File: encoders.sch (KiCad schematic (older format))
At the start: 40 parts

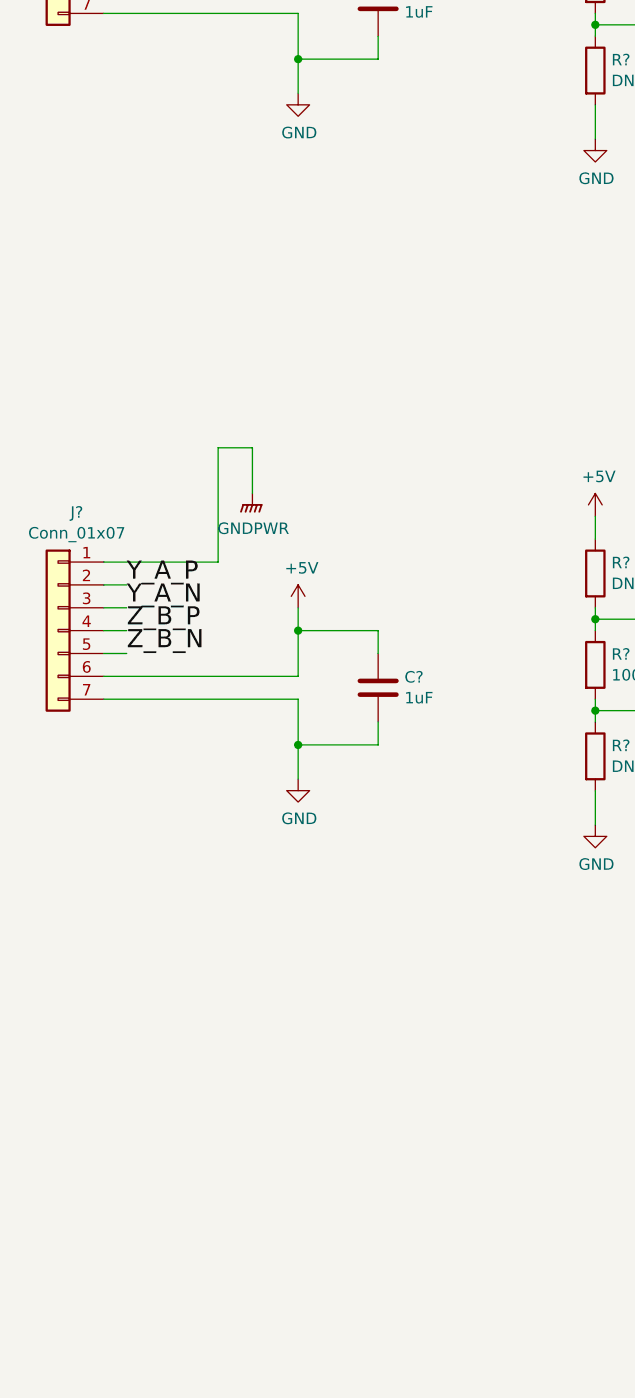
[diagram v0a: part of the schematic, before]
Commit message: Added motor feedback to stm32. added comms/boot to stm32
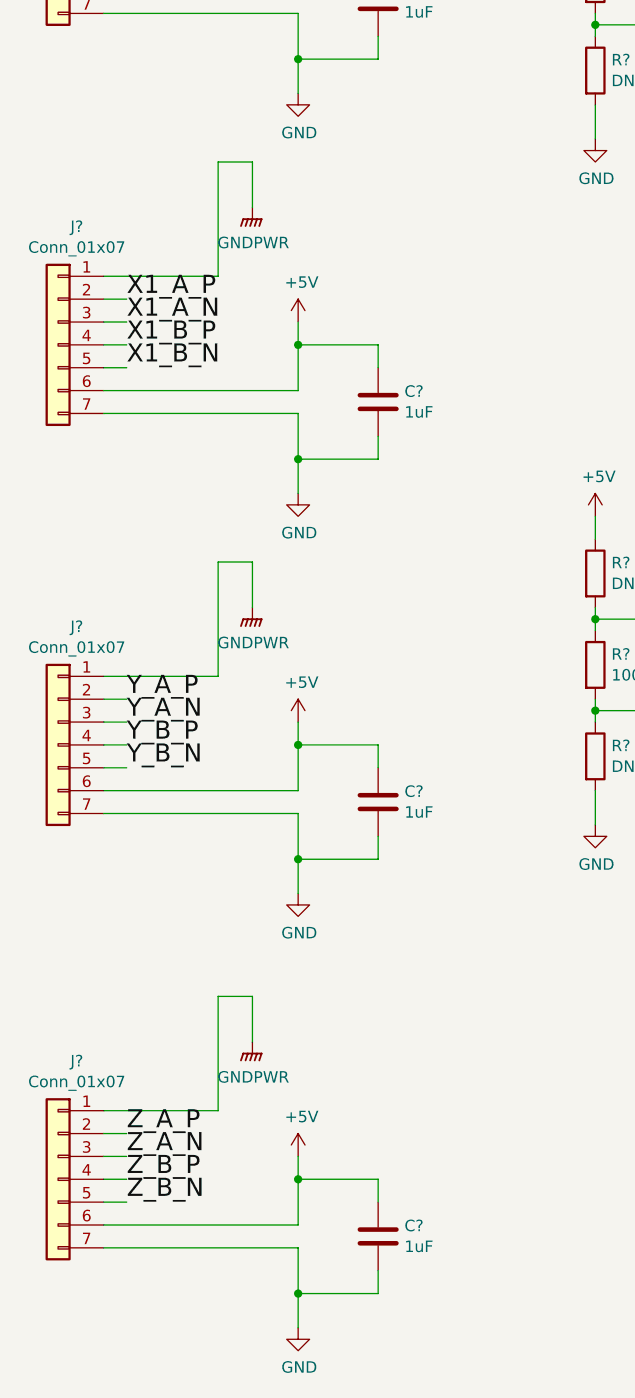
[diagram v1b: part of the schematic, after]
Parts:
- added C? (x2): 1uF, symbol Device:C
- added J? (x2): Conn_01x07, symbol Connector_Generic:Conn_01x07
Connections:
- net +5V: now also C?.1, C?.1, J?.6 (Pin_6), J?.6 (Pin_6)
- net GND: now also C?.2, C?.2, J?.7 (Pin_7), J?.7 (Pin_7)
- net GNDPWR: now also J?.1 (Pin_1), J?.1 (Pin_1)
- net X1_A_N: now also J?.3 (Pin_3)
- net X1_A_P: now also J?.2 (Pin_2)
- net X1_B_N: now also J?.5 (Pin_5)
- net X1_B_P: now also J?.4 (Pin_4)
- net Y_B_N: now also J?.5 (Pin_5)
- net Y_B_P: now also J?.4 (Pin_4)
- net Z_A_N: now also J?.3 (Pin_3)
- net Z_A_P: now also J?.2 (Pin_2)
- net Z_B_N: now also J?.5 (Pin_5); no longer J?.5 (Pin_5)
- net Z_B_P: now also J?.4 (Pin_4); no longer J?.4 (Pin_4)
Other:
- moved on the sheet: C?, J?

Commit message: cleaned encoder rx. removed PU from CoP rst. misc other CoP updates
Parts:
- C?: value C -> 0.1uF; footprint (none) -> Capacitor_SMD:C_0603_1608Metric_Pad1.05x0.95mm_HandSolder
- C?: value C -> 0.1uF
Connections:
- net GND: now also U?.8 (GND), U?.8 (GND)
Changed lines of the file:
@@
 P 10650 700
 F 0 "C?" H 10765 746 50  0000 L CNN
-F 1 "C" H 10765 655 50  0000 L CNN
-F 2 "" H 10688 550 50  0001 C CNN
+F 1 "0.1uF" H 10765 655 50  0000 L CNN
+F 2 "Capacitor_SMD:C_0603_1608Metric_Pad1.05x0.95mm_HandSolder" H 10688 550 50  0001 C CNN
 F 3 "~" H 10650 700 50  0001 C CNN
 	1    10650 700
@@
 P 10650 3700
 F 0 "C?" H 10765 3746 50  0000 L CNN
-F 1 "C" H 10765 3655 50  0000 L CNN
+F 1 "0.1uF" H 10765 3655 50  0000 L CNN
 F 2 "" H 10688 3550 50  0001 C CNN
 F 3 "~" H 10650 3700 50  0001 C CNN
@@
 Wire Wire Line
 	1600 6450 1100 6450
+Wire Wire Line
+	9450 6100 9450 6250
+Wire Wire Line
+	9450 3100 9450 3250
 $EndSCHEMATC

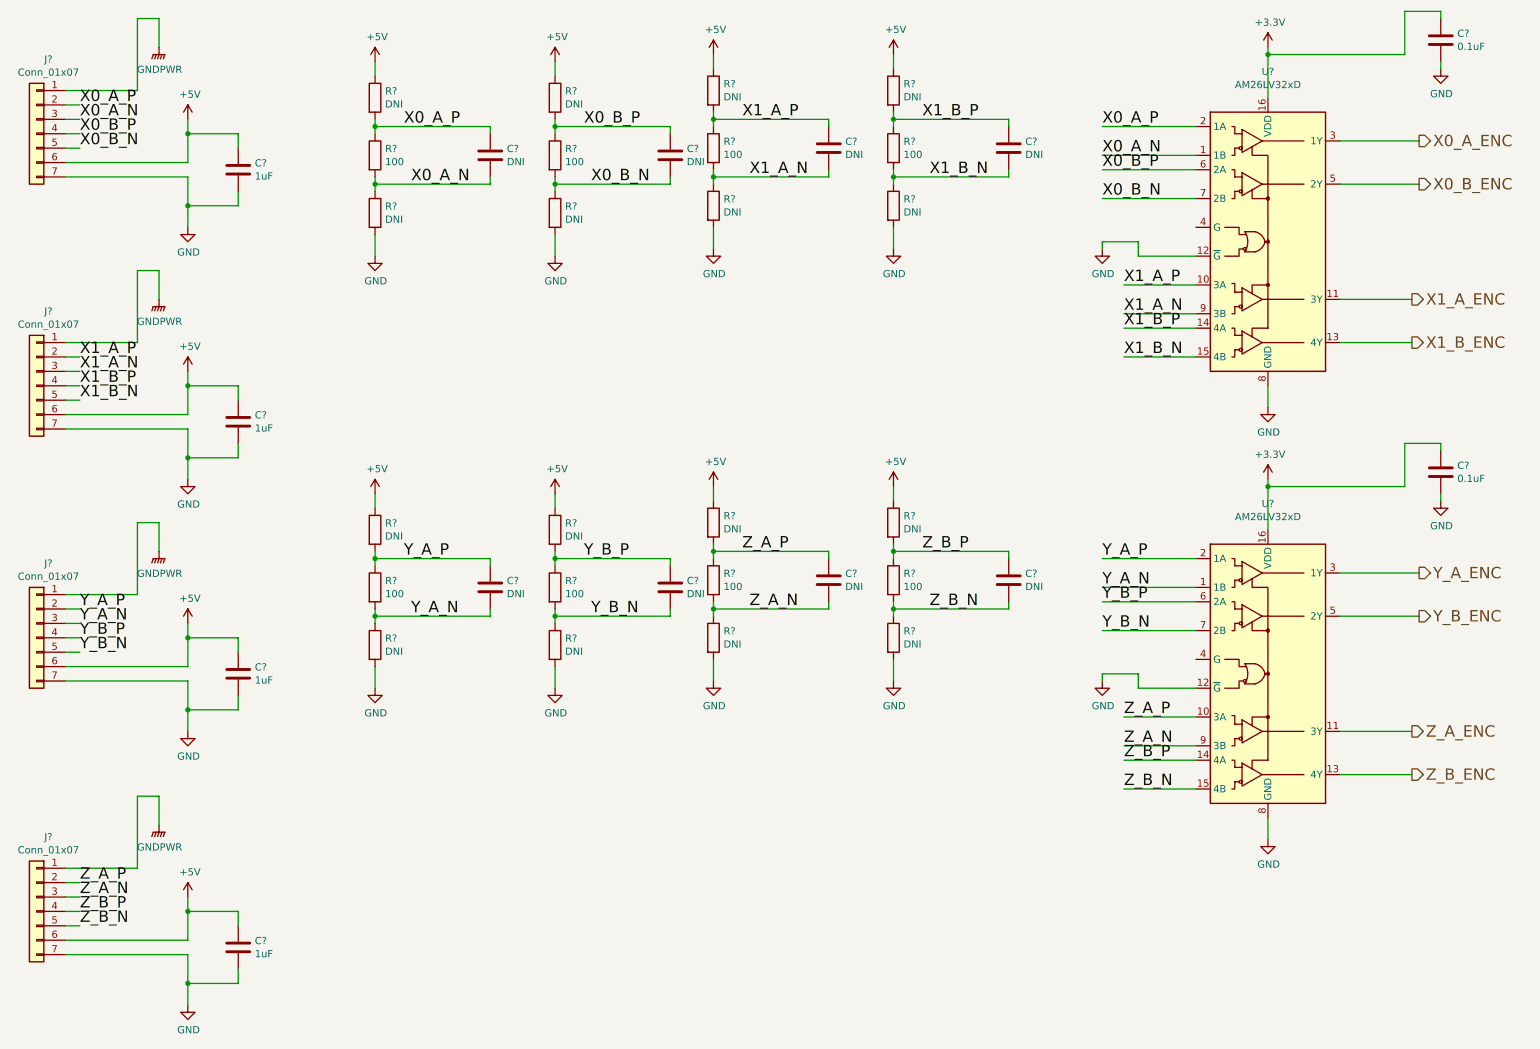
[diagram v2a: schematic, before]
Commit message: connected CoP + mP SPI. pushed updated into layout
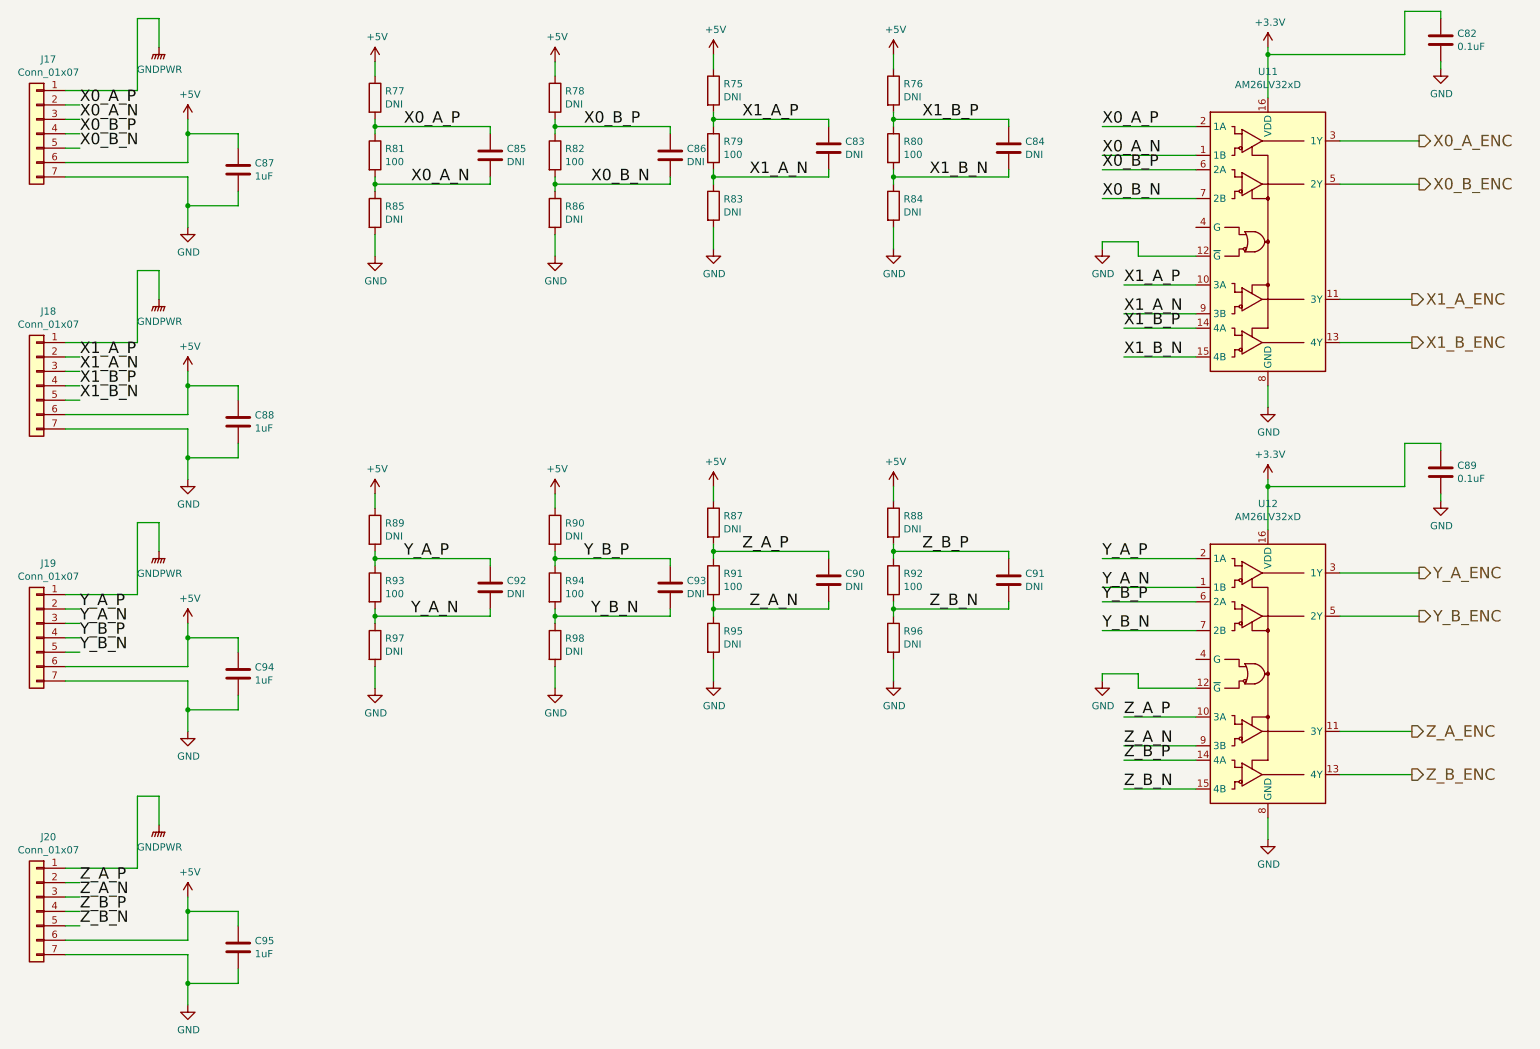
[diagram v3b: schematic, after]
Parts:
- gave numbers to parts that had none: 44
